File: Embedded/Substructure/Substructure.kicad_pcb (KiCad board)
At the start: 2 copper layers, 45 x 21 mm, 18 parts, among them J1 USB, J2 Pogo Pins, J3 JST [D], J4 JST [D], U1 Comms Link Expansion, U2 TCA9535RTWR, U3 TOF 0, U4 TOF 1, U5 FFC [U], U6 Display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

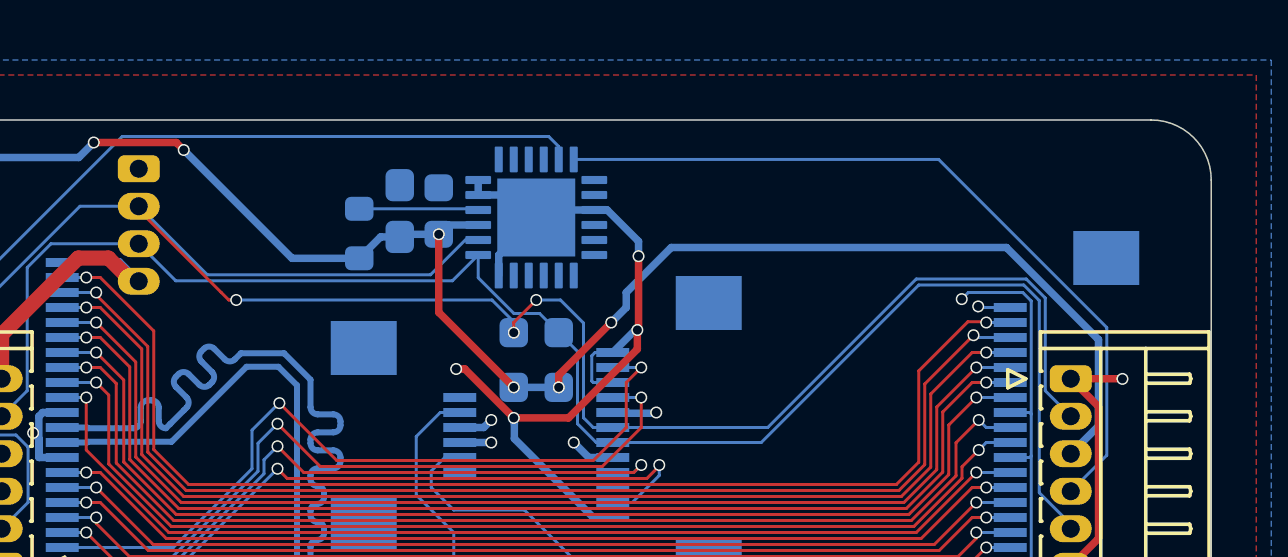
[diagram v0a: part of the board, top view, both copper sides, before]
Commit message: Added Mount Holes
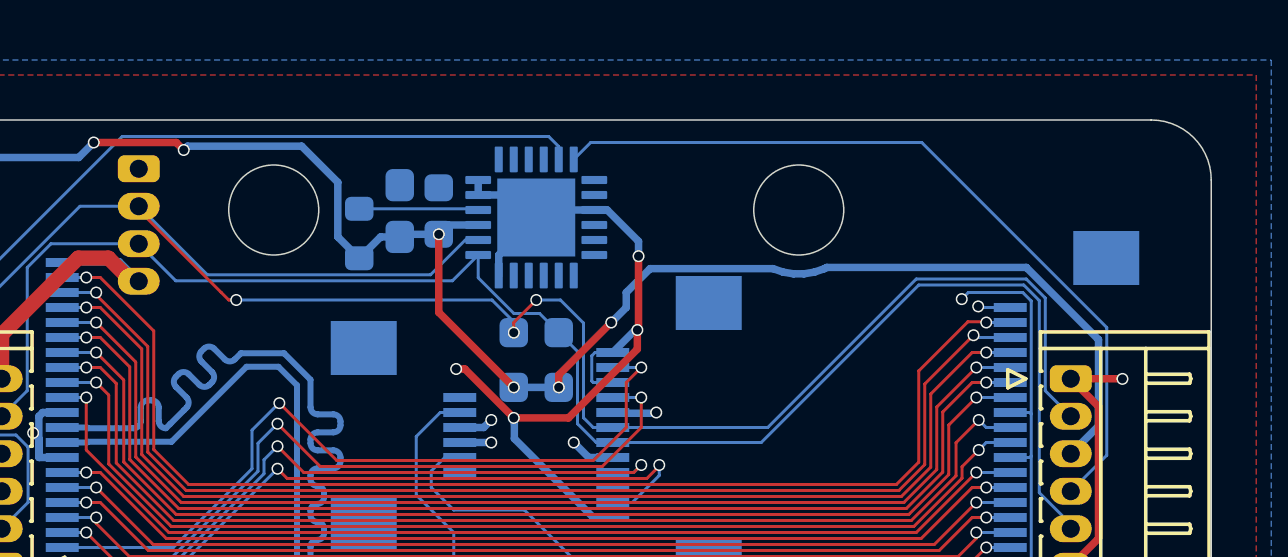
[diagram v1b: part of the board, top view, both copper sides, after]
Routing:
- net +3V3: track 66.3 -> 67.0 mm
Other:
- outline, holes or cut-outs redrawn
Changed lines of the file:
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@@
+		(layer "Edge.Cuts")
+	)
+	(gr_circle
+		(center 158.75 92.5)
+		(end 158.75 91)
+		(stroke
+			(width 0.05)
+			(type default)
+		)
+		(fill none)
 		(layer "Edge.Cuts")
 	)
@@
 		(layer "Edge.Cuts")
 	)
+	(gr_circle
+		(center 141.25 92.5)
+		(end 141.25 91)
+		(stroke
+			(width 0.05)
+			(type default)
+		)
+		(fill none)
+		(layer "Edge.Cuts")
+	)
 	(segment
 		(start 149.25 99.43)
@@
 	)
 	(segment
+		(start 152.5 96.25)
+		(end 153 95.75)
+		(width 0.25)
+		(layer "B.Cu")
+		(net 2)
+	)
+	(segment
+		(start 158.225958 94.569408)
+		(end 158.573714 94.627438)
+		(width 0.25)
+		(layer "B.Cu")
+		(net 2)
+	)
+	(segment
+		(start 159.607514 94.454927)
+		(end 159.682912 94.414124)
+		(width 0.25)
+		(layer "B.Cu")
+		(net 2)
+	)
+	(segment
 		(start 132.1825 101.875001)
 		(end 129.25 98.942501)
@@
 	)
 	(segment
-		(start 154.5 93.75)
-		(end 165.671751 93.75)
+		(start 166.335876 94.414124)
+		(end 168.7425 96.820749)
 		(width 0.25)
 		(layer "B.Cu")
@@
 	)
 	(segment
-		(start 153 95.25)
-		(end 154.5 93.75)
+		(start 157.892486 94.454927)
+		(end 158.225958 94.569408)
 		(width 0.25)
 		(layer "B.Cu")
@@
 	)
 	(segment
+		(start 153 95.75)
+		(end 153 95.25)
+		(width 0.25)
+		(layer "B.Cu")
+		(net 2)
+	)
+	(segment
+		(start 159.274042 94.569408)
+		(end 159.607514 94.454927)
+		(width 0.25)
+		(layer "B.Cu")
+		(net 2)
+	)
+	(segment
 		(start 131 90.75)
 		(end 134.75 90.75)
@@
 	)
 	(segment
-		(start 165.671751 93.75)
-		(end 168.7425 96.820749)
-		(width 0.25)
-		(layer "B.Cu")
-		(net 2)
-	)
-	(segment
-		(start 153 95.75)
-		(end 153 95.25)
+		(start 138.25 90.5)
+		(end 138.376361 90.373639)
 		(width 0.25)
 		(layer "B.Cu")
@@
 	)
 	(segment
-		(start 138.25 90.5)
-		(end 141.86 94.11)
+		(start 168.7425 96.820749)
+		(end 168.7425 99.7)
 		(width 0.25)
 		(layer "B.Cu")
@@
 	)
 	(segment
+		(start 153.795073 94.454927)
+		(end 157.892486 94.454927)
+		(width 0.25)
+		(layer "B.Cu")
+		(net 2)
+	)
+	(segment
+		(start 143.38473 91.576312)
+		(end 143.38473 93.39473)
+		(width 0.25)
+		(layer "B.Cu")
+		(net 2)
+	)
+	(segment
 		(start 144.812499 93.397501)
 		(end 144.1 94.11)
@@
 	)
 	(segment
+		(start 138.376361 90.373639)
+		(end 142.182057 90.373639)
+		(width 0.25)
+		(layer "B.Cu")
+		(net 2)
+	)
+	(segment
 		(start 147.06 93)
 		(end 146.75 93.31)
@@
 	)
 	(segment
-		(start 141.86 94.11)
+		(start 158.926286 94.627438)
+		(end 159.274042 94.569408)
+		(width 0.25)
+		(layer "B.Cu")
+		(net 2)
+	)
+	(segment
+		(start 143.38473 93.39473)
 		(end 144.1 94.11)
+		(width 0.25)
+		(layer "B.Cu")
+		(net 2)
+	)
+	(segment
+		(start 142.182057 90.373639)
+		(end 143.38473 91.576312)
 		(width 0.25)
 		(layer "B.Cu")
@@
 	)
 	(segment
-		(start 168.7425 96.820749)
-		(end 168.7425 99.7)
+		(start 153 95.25)
+		(end 153.795073 94.454927)
+		(width 0.25)
+		(layer "B.Cu")
+		(net 2)
+	)
+	(segment
+		(start 159.682912 94.414124)
+		(end 166.335876 94.414124)
 		(width 0.25)
 		(layer "B.Cu")
@@
 	)
 	(segment
+		(start 158.573714 94.627438)
+		(end 158.926286 94.627438)
+		(width 0.25)
+		(layer "B.Cu")
+		(net 2)
+	)
+	(segment
 		(start 129.25 93)
 		(end 129.25 91.9)
@@
 		(net 2)
 	)
-	(segment
-		(start 152.5 96.25)
-		(end 153 95.75)
-		(width 0.25)
-		(layer "B.Cu")
-		(net 2)
-	)
 	(via
 		(at 151.25 100.25)
@@
 	)
 	(segment
-		(start 163.415 90.815)
+		(start 151.815 90.25)
 		(end 151.25 90.815)
 		(width 0.1)
@@
 	)
 	(segment
+		(start 167.8175 101.874999)
+		(end 169.0175 100.674999)
+		(width 0.1)
+		(layer "B.Cu")
+		(net 18)
+	)
+	(segment
+		(start 162.85 90.25)
+		(end 151.815 90.25)
+		(width 0.1)
+		(layer "B.Cu")
+		(net 18)
+	)
+	(segment
 		(start 169.0175 96.4175)
-		(end 163.415 90.815)
+		(end 162.85 90.25)
 		(width 0.1)
 		(layer "B.Cu")
@@
 		(width 0.1)
 		(layer "B.Cu")
-		(net 18)
-	)
-	(segment
-		(start 167.8175 101.874999)
-		(end 169.0175 100.674999)
-		(width 0.1)
-		(layer "B.Cu")

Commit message: Added Photoresistors
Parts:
- added C3: 1uF, Resistor_SMD:R_0603_1608Metric, B.Cu at (162.0, 92.0)
- added C4: 1uF, Resistor_SMD:R_0603_1608Metric, B.Cu at (168.8, 91.5)
- added C5: 10uF, Capacitor_SMD:C_0603_1608Metric, B.Cu at (167.2, 91.5)
- added R4: R_Photo, Photoresistor:Photoresistor Aliexpress, F.Cu at (131.0, 109.0)
- added R5: R_Photo, Photoresistor:Photoresistor Aliexpress, F.Cu at (169.0, 109.0)
- added R6: 10K, Resistor_SMD:R_0603_1608Metric_Pad0.98x0.95mm_HandSolder, B.Cu at (134.5, 108.1)
- added R7: 10K, Resistor_SMD:R_0603_1608Metric_Pad0.98x0.95mm_HandSolder, B.Cu at (165.5, 108.1)
- added REF**: Logo_20mm, Logo:Logo_20mm, F.Cu at (150.0, 100.0)
- added U8: AP7366-33W5-7, AP7366-SOT25:AP7366, B.Cu at (164.5, 92.0)
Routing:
- net +3V3: track 67.0 -> 89.3 mm, vias 6 -> 10
- net EXP Comms A: track 9.39 -> 31.2 mm, vias 0 -> 4
- net EXP Comms B: track 8.02 -> 29.8 mm, vias 0 -> 4
- net GND: track 53.0 -> 68.6 mm, vias 7 -> 12
- net SDA: track 72.3 -> 63.9 mm, vias 3 -> 4
- net XShut 1: track 26.5 -> 31.5 mm, vias 0 -> 2
- net +5V: track 23.2 -> 26.8 mm, vias 7 -> 8
- net SCL: track 55.1 -> 55.6 mm
- net XShut 0: track 29.1 -> 29.2 mm, vias 0 -> 2
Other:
- outline, holes or cut-outs redrawn

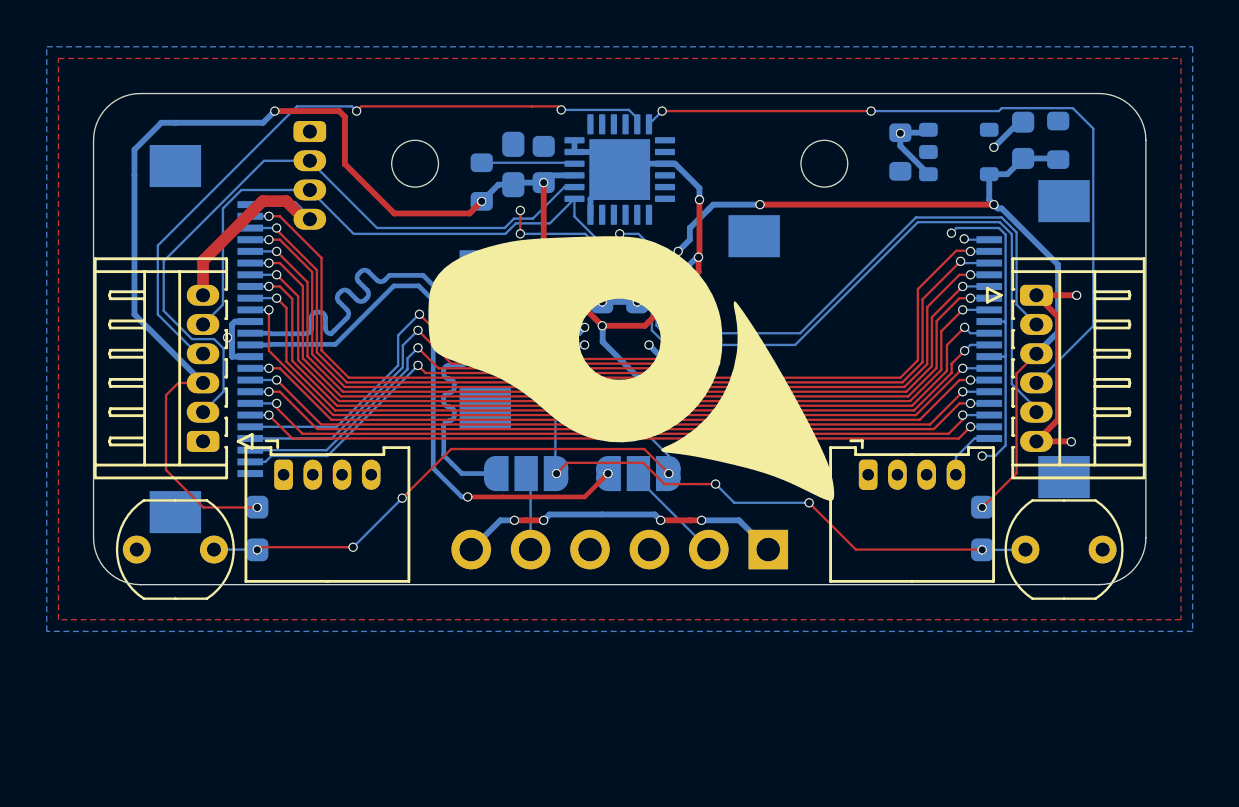
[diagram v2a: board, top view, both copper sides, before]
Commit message: Added Routing for Pins
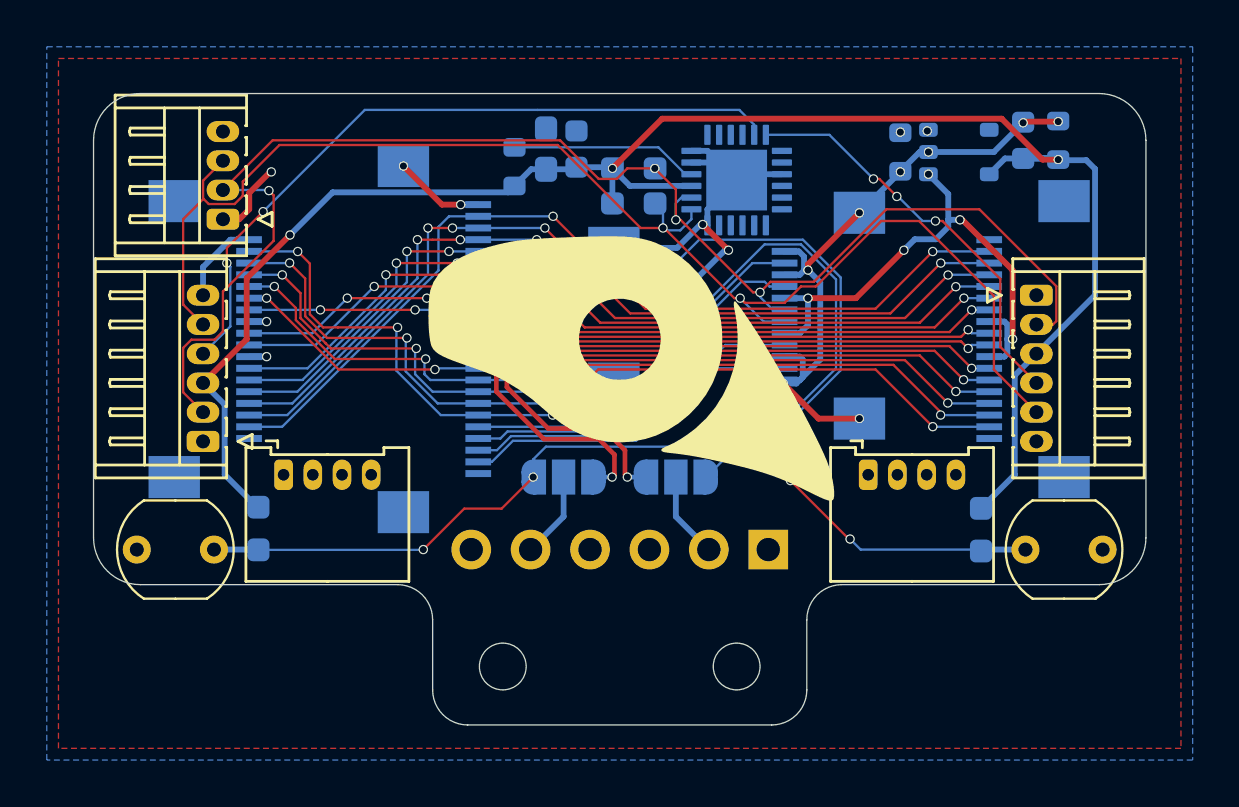
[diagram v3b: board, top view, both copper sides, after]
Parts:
- added U9: Display, FFC_Connector:FFC Aliexpress 0.5mm 18P, B.Cu at (133.2, 100.0)
- J1: moved to F.Cu
- moved R4 38.0 mm to (169.0, 109.0), turned to 0 degrees
- moved R5 38.0 mm to (131.0, 109.0), turned to 180 degrees
- moved R6 31.0 mm to (165.4, 108.2)
- moved R7 30.9 mm to (134.6, 108.1)
- moved U7 9.75 mm to (143.0, 100.0)
- moved U1 5.59 mm to (152.0, 99.0)
- moved J1 5.28 mm to (133.0, 94.9), turned to 90 degrees
- moved U2 5.02 mm to (155.0, 93.2)
- moved R2 4.99 mm to (150.6, 92.7), turned to 0 degrees
- moved U5 4.61 mm to (158.0, 99.0)
- moved R1 3.30 mm to (150.6, 94.2), turned to 0 degrees
- moved JP1 1.61 mm to (152.4, 105.9), turned to 0 degrees
- moved JP2 1.61 mm to (147.6, 105.9)
- moved C1 1.55 mm to (148.2, 91.9)
- moved C2 1.55 mm to (146.8, 91.9)
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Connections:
- JP1 pad 1: EXP Comms A -> USB +
- JP1 pad 3: USB + -> EXP Comms A
- JP2 pad 1: EXP Comms B -> USB -
- JP2 pad 3: USB - -> EXP Comms B
- U1 pad : (no net) -> GND
- U5 pad : (no net) -> GND
- U6 pad : (no net) -> GND
- U7 pad : (no net) -> GND
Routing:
- net USB -: track 27.5 -> 12.5 mm, vias 0 -> 2
- net GND: track 68.6 -> 53.7 mm
- net XShut 1: track 31.5 -> 17.7 mm, vias 2 -> 3
- net USB +: track 24.7 -> 11.6 mm
- net EXP Comms B: track 29.8 -> 41.9 mm, vias 4 -> 2
- net +3V3: track 89.3 -> 78.0 mm, vias 10 -> 3
- net GPIO 3: track 24.3 -> 14.8 mm, vias 2 -> 0
- net GPIO 0: track 26.0 -> 17.0 mm, vias 2 -> 0
- net GPIO 2: track 22.9 -> 15.0 mm, vias 2 -> 0
- net EXP Comms A: track 31.2 -> 39.1 mm, vias 4 -> 2
- net GPIO 1: track 24.8 -> 17.0 mm, vias 2 -> 0
- net Exp 0: track 32.2 -> 38.8 mm, vias 2 -> 4
- net Exp 1: track 32.7 -> 37.6 mm, vias 2 -> 4
- net SCL: track 55.6 -> 60.0 mm, vias 0 -> 2
- net +5V: track 26.8 -> 31.2 mm, vias 8 -> 13
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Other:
- board size 45 x 21 mm -> 45 x 27 mm
